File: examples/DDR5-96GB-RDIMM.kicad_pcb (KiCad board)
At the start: 8 copper layers, 133.3 x 30 mm, 107 parts, among them J1 DDR5-288, U1 4GB DDR5, U10 4GB DDR5, U11 4GB DDR5, U12 4GB DDR5, U13 4GB DDR5, U14 4GB DDR5, U15 4GB DDR5, U16 4GB DDR5, U17 4GB DDR5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

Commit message: added improved collab software
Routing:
- net VDD: track 128.7 -> 1567.4 mm, vias 149 -> 197
- net VSS: track 17.3 -> 1056.3 mm, vias 300 -> 606
- net VDDQ: track 125.7 -> 895.3 mm
- net VPP: track 126.5 -> 383.8 mm, vias 1 -> 7
- net DQ48: track 26.9 -> 17.3 mm, vias 4 -> 2
- net DQ7: track 30.2 -> 20.6 mm, vias 4 -> 2
- net DQ63: track 26.7 -> 17.0 mm, vias 4 -> 2
- net DQ47: track 42.9 -> 33.3 mm, vias 4 -> 2
- net DQ39: track 40.4 -> 30.7 mm, vias 4 -> 2
- net DQ31: track 37.9 -> 28.2 mm, vias 4 -> 2
- net DQ23: track 35.3 -> 25.7 mm, vias 4 -> 2
- net DQ15: track 32.8 -> 23.1 mm, vias 4 -> 2
- net DQ30: track 36.6 -> 28.2 mm, vias 4 -> 2
- net DQ14: track 31.5 -> 23.1 mm, vias 4 -> 2
- net DQ22: track 34.0 -> 25.7 mm, vias 4 -> 2
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
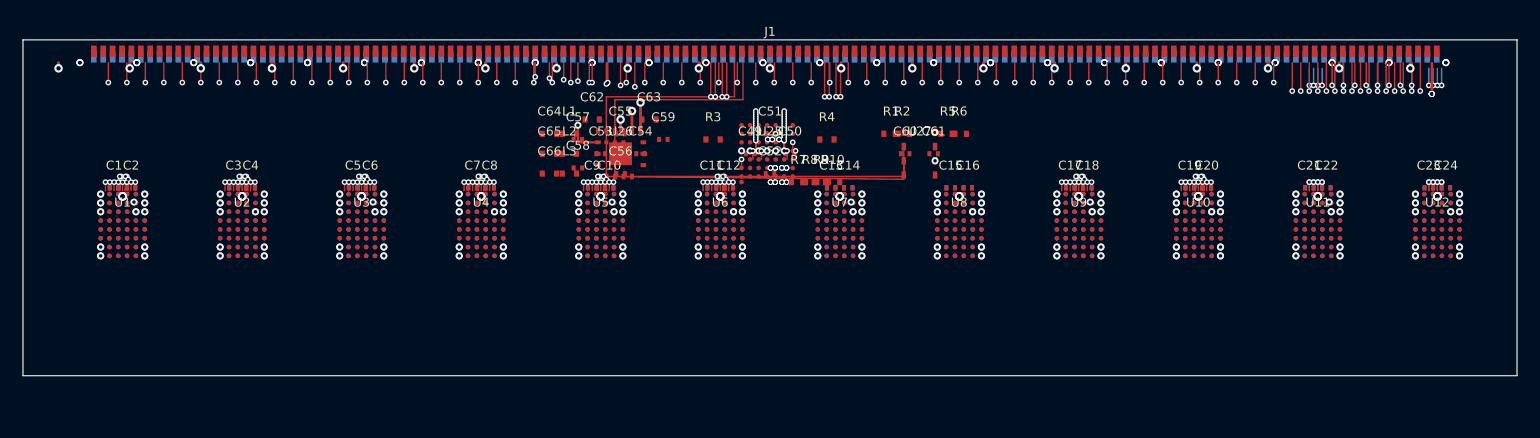
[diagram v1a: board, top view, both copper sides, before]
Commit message: added more validation tests, collaborative session, screenshots and better render support.
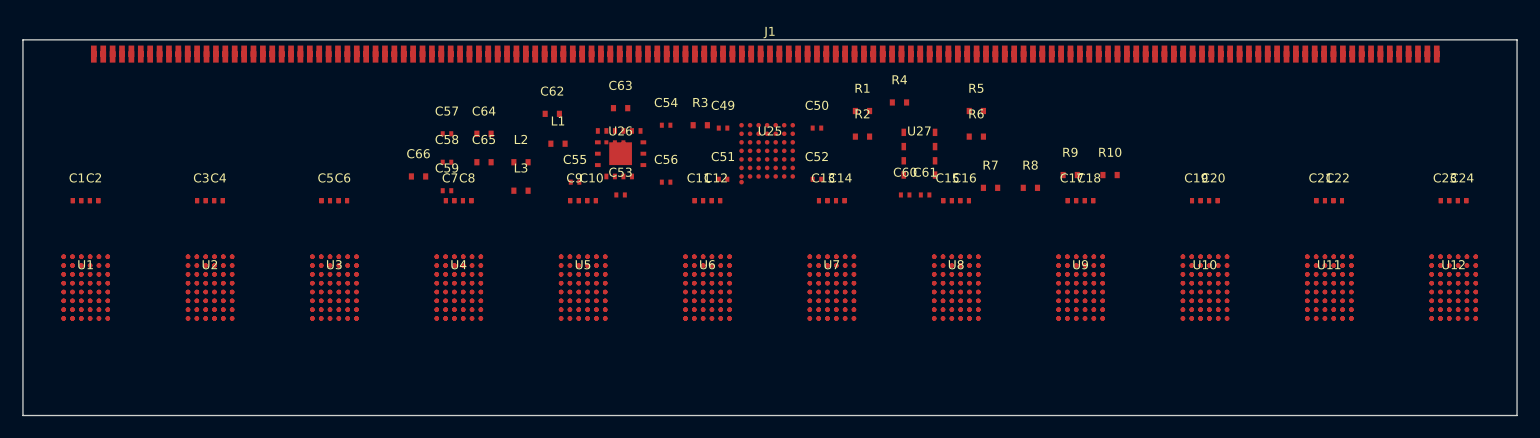
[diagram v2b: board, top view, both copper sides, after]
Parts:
- moved R10 24.8 mm to (97.0, 12.1)
- moved R9 22.2 mm to (93.5, 12.1)
- moved C59 19.8 mm to (37.8, 13.5)
- moved R8 19.7 mm to (89.9, 13.2)
- moved R7 17.2 mm to (86.4, 13.2)
- moved C57 11.7 mm to (37.8, 8.38)
- moved C58 11.7 mm to (37.8, 10.9)
- moved C66 11.7 mm to (35.3, 12.2)
- moved R4 7.27 mm to (78.2, 5.59)
- moved U1 6.49 mm to (5.59, 22.1)
- moved U13 6.49 mm to (5.59, 22.1)
- moved U14 6.28 mm to (16.7, 22.1)
- moved U2 6.28 mm to (16.7, 22.1)
- moved U15 6.10 mm to (27.8, 22.1)
- moved U3 6.10 mm to (27.8, 22.1)
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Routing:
- net VDD: track 1567.4 -> 0.00 mm, vias 197 -> 0
- net VSS: track 1056.3 -> 0.00 mm, vias 606 -> 0
- net VDDQ: track 895.3 -> 0.00 mm, vias 1 -> 0
- net VPP: track 383.8 -> 0.00 mm, vias 7 -> 0
- net CAA0: track 236.6 -> 0.00 mm, vias 2 -> 0
- net CAA1: track 236.4 -> 0.00 mm, vias 2 -> 0
- net CAA2: track 236.2 -> 0.00 mm, vias 2 -> 0
- net CAA3: track 236.0 -> 0.00 mm, vias 2 -> 0
- net CAA4: track 235.8 -> 0.00 mm, vias 2 -> 0
- net CAA5: track 235.6 -> 0.00 mm, vias 2 -> 0
- net CAA6: track 235.4 -> 0.00 mm, vias 2 -> 0
- net CAA7: track 235.2 -> 0.00 mm, vias 2 -> 0
- net CAA8: track 235.0 -> 0.00 mm, vias 2 -> 0
- net CAA9: track 234.8 -> 0.00 mm, vias 2 -> 0
- net CAA10: track 234.6 -> 0.00 mm, vias 2 -> 0
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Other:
- board size 133.3 x 30 mm -> 133.3 x 33.5 mm
- copper layers 8 -> 6
